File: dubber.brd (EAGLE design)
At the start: 52 x 55.5 mm, 31 parts, among them IC1 LM324N, P1-G TPSQPAD1-13Y, P1-S TPSQPAD1-13Y, P2-G TPSQPAD1-13Y, P2-S TPSQPAD1-13Y, P3-G TPSQPAD1-13Y, P3-S TPSQPAD1-13Y

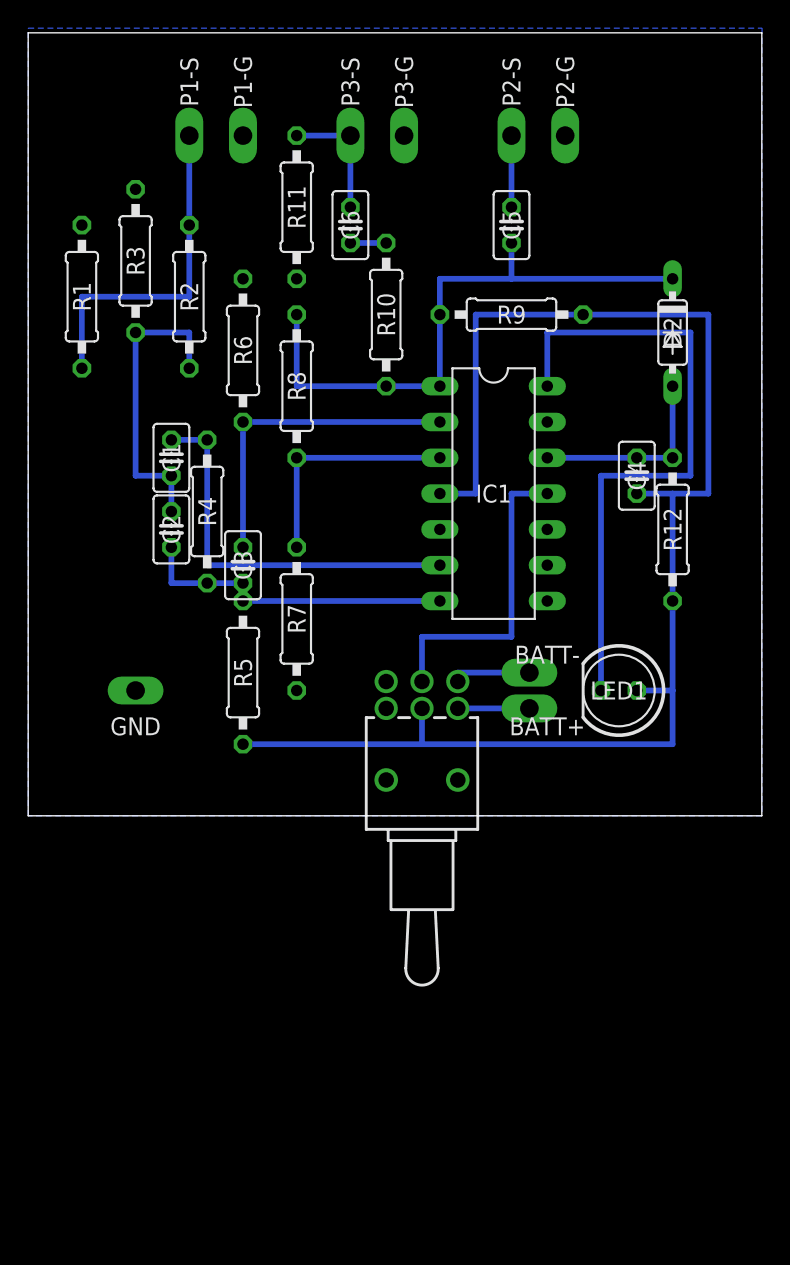
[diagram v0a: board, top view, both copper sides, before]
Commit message: ocd round 1, straighten resistors and miter corners
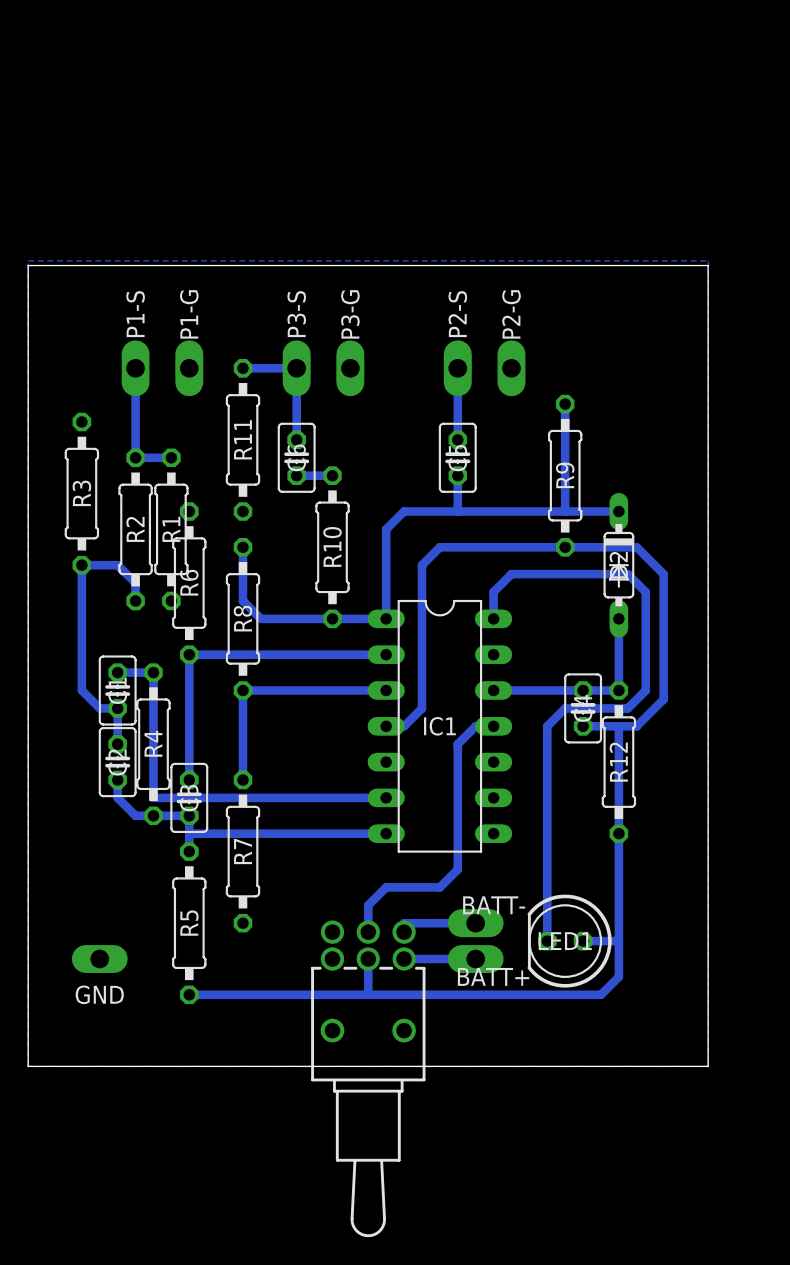
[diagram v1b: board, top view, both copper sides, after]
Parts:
- moved GND 19.2 mm to (5.08, 7.62)
- moved BATT- 18.2 mm to (31.8, 10.2)
- moved LED1 18.2 mm to (38.1, 8.89)
- moved R5 18.2 mm to (11.4, 10.2)
- moved S1 18.2 mm to (24.1, 2.54)
- moved BATT+ 18.2 mm to (31.8, 7.62)
- moved R1 17.7 mm to (10.2, 38.1), turned to 90 degrees
- moved P1-G 16.9 mm to (11.4, 49.5)
- moved P1-S 16.9 mm to (7.62, 49.5)
- moved P2-G 16.9 mm to (34.3, 49.5)
- moved P3-G 16.9 mm to (22.9, 49.5)
- moved C2 16.9 mm to (6.35, 21.6)
- moved C3 16.9 mm to (11.4, 19.1)
- moved IC1 16.9 mm to (29.2, 24.1)
- moved P2-S 16.9 mm to (30.5, 49.5)
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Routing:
- net N$17: track 24.1 -> 8.89 mm
- net N$10: track 41.9 -> 48.0 mm
- net V+: track 102.9 -> 100.9 mm
- net N$12: track 45.7 -> 44.0 mm
- net N$1: track 21.6 -> 20.1 mm
- net V-: track 22.2 -> 21.3 mm
- net N$2: track 22.9 -> 23.4 mm
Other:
- board size 52 x 55.5 mm -> 48.2 x 56.8 mm

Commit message: ocd round 2, schematic cleanup and moving components into space
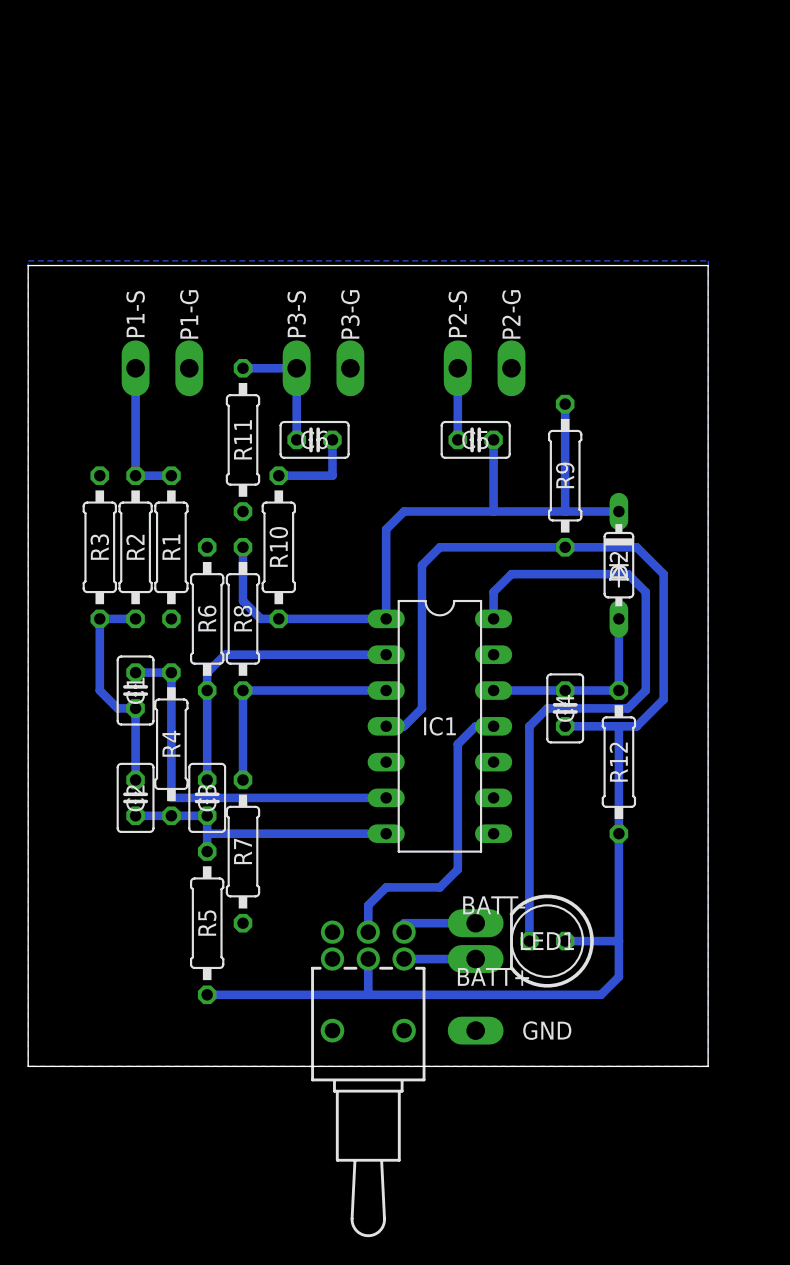
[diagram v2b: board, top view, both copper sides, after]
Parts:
- moved GND 27.1 mm to (31.8, 2.54)
- moved R3 4.02 mm to (5.08, 36.8)
- moved R10 3.81 mm to (17.8, 36.8)
- moved C2 2.84 mm to (7.62, 19.1)
- moved R6 2.84 mm to (12.7, 31.8)
- moved C5 1.80 mm to (31.8, 44.5), turned to 180 degrees
- moved C6 1.80 mm to (20.3, 44.5), turned to 180 degrees
- moved LED1 1.27 mm to (36.8, 8.89)
- moved R1 1.27 mm to (10.2, 36.8)
- moved R2 1.27 mm to (7.62, 36.8)
- moved C1 1.27 mm to (7.62, 26.7)
- moved C3 1.27 mm to (12.7, 19.1)
- moved R4 1.27 mm to (10.2, 22.9)
- moved R5 1.27 mm to (12.7, 10.2)
- moved C4 1.27 mm to (38.1, 25.4)
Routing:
- net N$1: track 20.1 -> 15.8 mm
- net N$3: track 2.54 -> 6.35 mm
- net N$2: track 23.4 -> 20.3 mm
- net N$10: track 48.0 -> 50.6 mm
- net N$18: track 22.9 -> 20.8 mm
- net N$17: track 8.89 -> 10.2 mm
- net N$16: track 27.9 -> 26.7 mm
- net N$12: track 44.0 -> 45.3 mm
- net V+: track 100.9 -> 102.2 mm

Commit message: tweaks again
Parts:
- removed BATT+, BATT-, P1-S, P2-S: TPSQPAD1-13Y, testpad:P1-13Y
- added +, -, INPUT, OUTPUT: TPSQPAD1-13Y, testpad:P1-13Y
- moved R11 8.13 mm to (21.6, 39.4)
- moved D2 6.35 mm to (35.6, 35.6)
- moved C4 5.24 mm to (39.4, 30.5)
- moved S1 3.81 mm to (20.3, 2.54)
- moved LED1 2.84 mm to (38.1, 11.4)
- moved C1 2.54 mm to (5.08, 26.7)
- moved C2 2.54 mm to (5.08, 19.1)
- moved C6 2.54 mm to (17.8, 44.5), turned to 0 degrees
- moved R12 2.54 mm to (39.4, 21.6)
- moved R9 2.29 mm to (39.4, 40.0)
- moved R4 1.90 mm to (8.26, 22.9)
- moved P2-G 1.27 mm to (35.6, 49.5)
- moved R2 1.27 mm to (6.35, 36.8)
- moved R3 1.27 mm to (3.81, 36.8)
- moved C3 1.27 mm to (11.4, 19.1)
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- renumbered P3-S to SLAVE
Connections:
- net N$14: now also OUTPUT.TP; no longer P2-S.TP
- net N$17: now also INPUT.TP; no longer P1-S.TP
- net N$4: now also +.TP; no longer BATT+.TP
- net N$5: now also -.TP; no longer BATT-.TP
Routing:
- net N$12: track 45.3 -> 26.8 mm
- net V+: track 102.2 -> 90.3 mm
- net N$10: track 50.6 -> 46.7 mm
- net N$3: track 6.35 -> 2.54 mm
- net N$4: track 5.08 -> 7.62 mm
- net N$9: track 14.0 -> 16.5 mm
- net N$5: track 5.71 -> 7.88 mm
- net V-: track 21.3 -> 23.4 mm
- net N$21: track 8.89 -> 7.62 mm
- net N$2: track 20.3 -> 21.6 mm
- net N$1: track 15.8 -> 14.5 mm
- net N$16: track 26.7 -> 27.2 mm
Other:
- board size 48.2 x 56.8 mm -> 47 x 54.3 mm
